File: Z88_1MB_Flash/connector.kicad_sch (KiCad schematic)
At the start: 5 parts, among them J1 Conn_Z88, U1 AM29F080-120EC

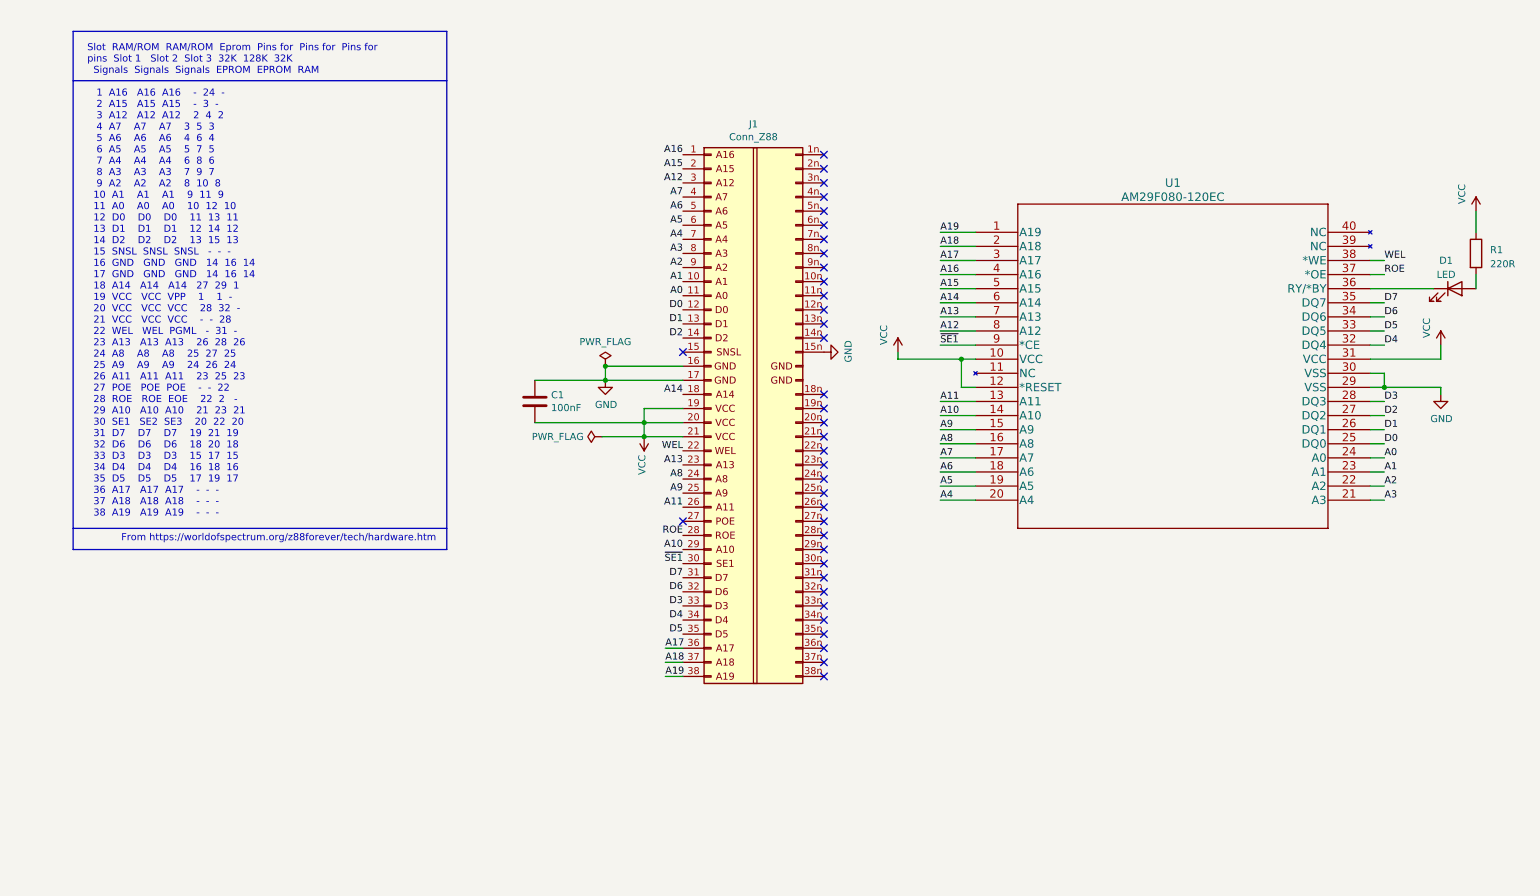
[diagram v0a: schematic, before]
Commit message: Add support for using 2 x 512KB SRAM chips instead of 1MB Flash.
The board can now be used either as a 1MB Flash store, 512KB RAM or 1MB
RAM.
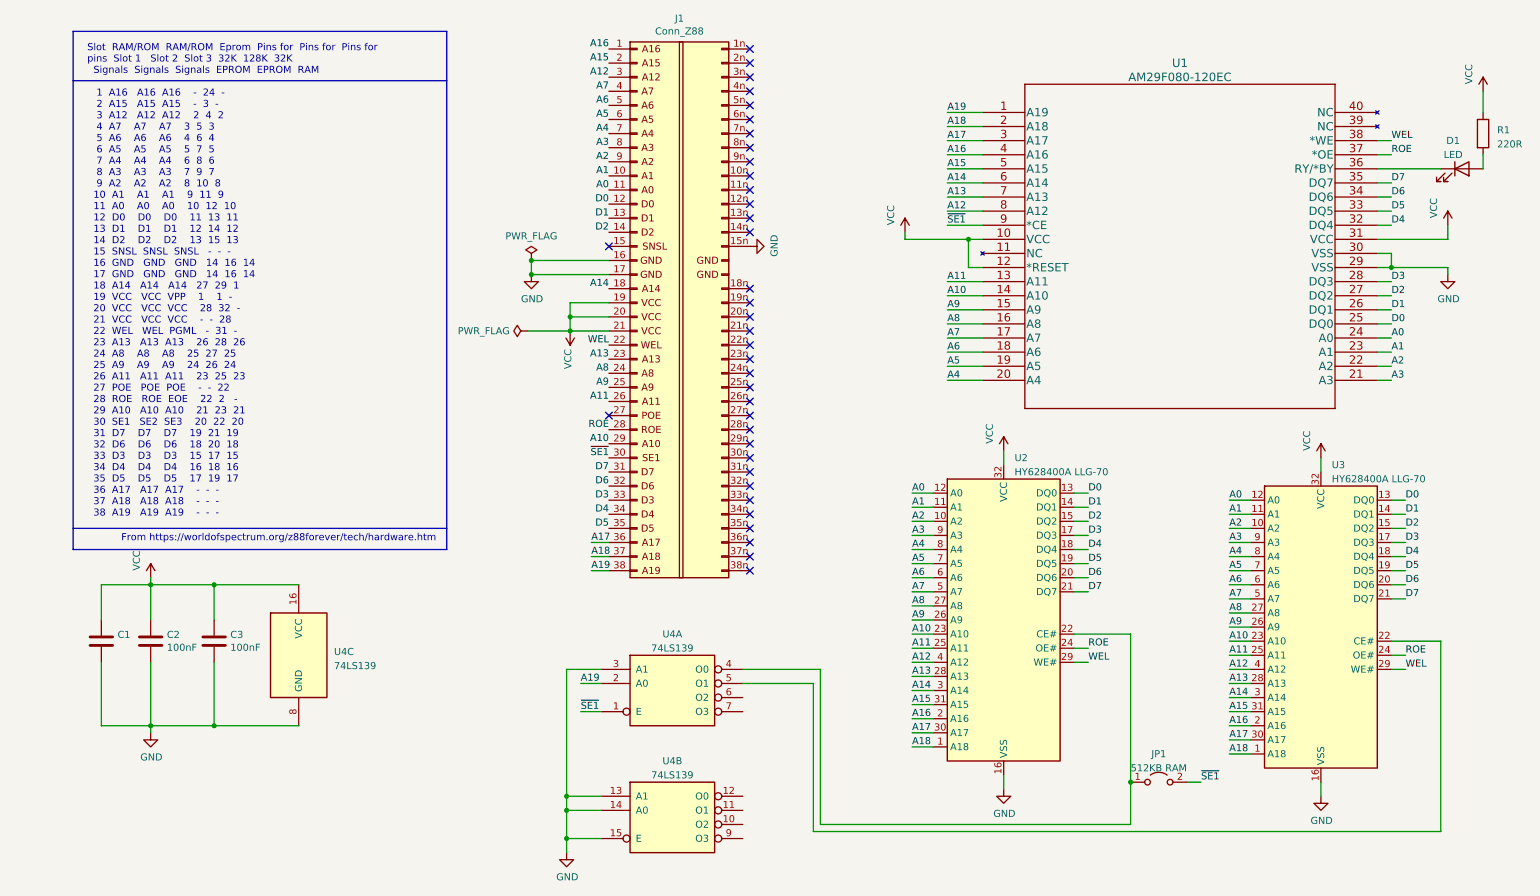
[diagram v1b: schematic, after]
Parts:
- added C2, C3: 100nF, Capacitor_SMD:C_1206_3216Metric, symbol Device:C
- added JP1: 512KB RAM, Jumper:SolderJumper-2_P1.3mm_Open_Pad1.0x1.5mm, symbol Jumper:Jumper_2_Open
- added U2, U3: HY628400A LLG-70, Package_SO:SSOP-32_11.305x20.495mm_P1.27mm, symbol Memory_RAM:AS6C4008-55PCN
- added U4: 74LS139, Package_SO:SO-16_3.9x9.9mm_P1.27mm, symbol 74xx:74LS139
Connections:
- net A0: now also U2.12 (A0), U3.12 (A0)
- net A1: now also U2.11 (A1), U3.11 (A1)
- net A10: now also U2.23 (A10), U3.23 (A10)
- net A11: now also U2.25 (A11), U3.25 (A11)
- net A12: now also U2.4 (A12), U3.4 (A12)
- net A13: now also U2.28 (A13), U3.28 (A13)
- net A14: now also U2.3 (A14), U3.3 (A14)
- net A15: now also U2.31 (A15), U3.31 (A15)
- net A16: now also U2.2 (A16), U3.2 (A16)
- net A17: now also U2.30 (A17), U3.30 (A17)
- net A18: now also U2.1 (A18), U3.1 (A18)
- net A19: now also U4.2 (A0)
- net A2: now also U2.10 (A2), U3.10 (A2)
- net A3: now also U2.9 (A3), U3.9 (A3)
- net A4: now also U2.8 (A4), U3.8 (A4)
- net A5: now also U2.7 (A5), U3.7 (A5)
- net A6: now also U2.6 (A6), U3.6 (A6)
- net A7: now also U2.5 (A7), U3.5 (A7)
- net A8: now also U2.27 (A8), U3.27 (A8)
- net A9: now also U2.26 (A9), U3.26 (A9)
- net D0: now also U2.13 (DQ0), U3.13 (DQ0)
- net D1: now also U2.14 (DQ1), U3.14 (DQ1)
- net D2: now also U2.15 (DQ2), U3.15 (DQ2)
- net D3: now also U2.17 (DQ3), U3.17 (DQ3)
- net D4: now also U2.18 (DQ4), U3.18 (DQ4)
- net D5: now also U2.19 (DQ5), U3.19 (DQ5)
- net D6: now also U2.20 (DQ6), U3.20 (DQ6)
- net D7: now also U2.21 (DQ7), U3.21 (DQ7)
- net GND: now also C1.2, C2.2, C3.2, U2.16 (VSS), U3.16 (VSS), U4.13 (A1), U4.14 (A0), U4.15 (E), U4.3 (A1), U4.8 (GND); no longer C1.1
- net ROE: now also U2.24 (OE#), U3.24 (OE#)
- net VCC: now also C1.1, C2.1, C3.1, U2.32 (VCC), U3.32 (VCC), U4.16 (VCC); no longer C1.2
- net WEL: now also U2.29 (WE#), U3.29 (WE#)
- net ~{SE1}: now also JP1.2 (B), U4.1 (E)
- new net: U3.22 (CE#), U4.5 (O1)
- new net: JP1.1 (A), U2.22 (CE#), U4.4 (O0)
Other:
- moved on the sheet: D1, J1, R1, U1
